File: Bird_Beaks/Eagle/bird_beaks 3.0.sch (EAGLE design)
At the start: 29 parts, among them U1 ADAFRUIT_ITSYBITSY_5V, X1 PHOENIX_508_3PIN, X10 PHOENIX_508_3PIN, X11 PHOENIX_508_4PIN, X2 PHOENIX_508_3PIN, X3 PHOENIX_508_3PIN, X4 PHOENIX_508_2PIN, X5 PHOENIX_508_4PIN, X6 PHOENIX_508_4PIN, X7 PHOENIX_508_3PIN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

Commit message: Revision for output
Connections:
- removed net HUMMINGIRD_OUTPUT: U1.SDA
- net HUMMINGBIRD_OUTPUT: now also U1.SDA
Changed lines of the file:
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@@
 <class number="0" name="Low Power" width="0.1524" drill="0.254">
 </class>
-<class number="1" name="High Power" width="0.762" drill="0.4826">
+<class number="1" name="High Power" width="1.27" drill="0.4826">
 </class>
 </classes>
@@
 </segment>
 </net>
-<net name="HUMMINGIRD_OUTPUT" class="0">
-<segment>
-<pinref part="U1" gate="G$1" pin="SDA"/>
-<wire x1="114.3" y1="134.62" x2="116.84" y2="134.62" width="0.1524" layer="91"/>
-<label x="116.84" y="134.62" size="1.778" layer="95"/>
-</segment>
-</net>
 <net name="TREECREEPER_OUTPUT" class="0">
 <segment>
@@
 </segment>
 </net>
-<net name="HUMMINGBIRD_OUTPUT" class="0">
-<segment>
-<pinref part="X9" gate="-2" pin="1"/>
-<wire x1="292.1" y1="205.74" x2="292.1" y2="195.58" width="0.1524" layer="91"/>
-<label x="289.56" y="198.12" size="1.778" layer="95" rot="R270"/>
-</segment>
-</net>
 <net name="12V" class="1">
 <segment>
@@
 </segment>
 </net>
+<net name="HUMMINGBIRD_OUTPUT" class="0">
+<segment>
+<pinref part="U1" gate="G$1" pin="SDA"/>
+<wire x1="114.3" y1="134.62" x2="116.84" y2="134.62" width="0.1524" layer="91"/>
+<label x="116.84" y="134.62" size="1.778" layer="95"/>
+</segment>
+<segment>
+<pinref part="X9" gate="-2" pin="1"/>
+<wire x1="292.1" y1="205.74" x2="292.1" y2="195.58" width="0.1524" layer="91"/>
+<label x="292.1" y="175.26" size="1.778" layer="95" rot="R90"/>
+</segment>
+</net>

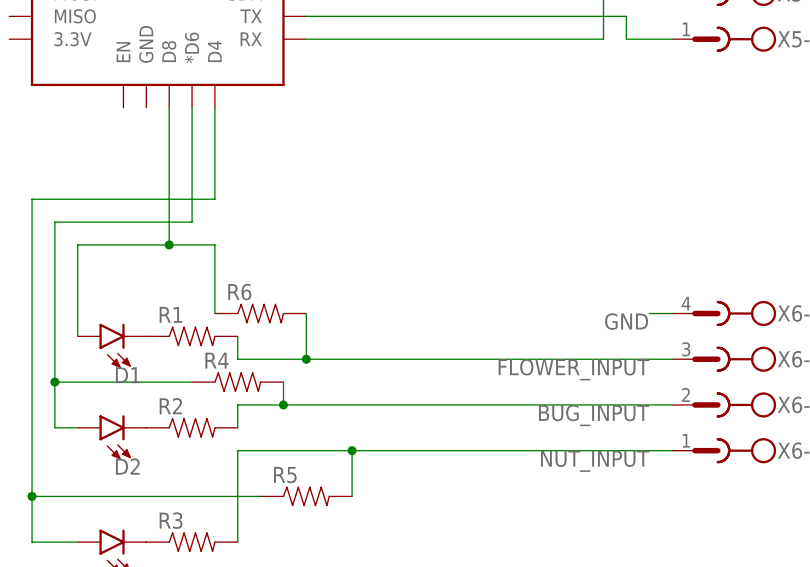
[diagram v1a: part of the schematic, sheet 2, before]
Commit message: completed the attractor sequence
fully flushed out the attractor sequence so that it will pulse on and off
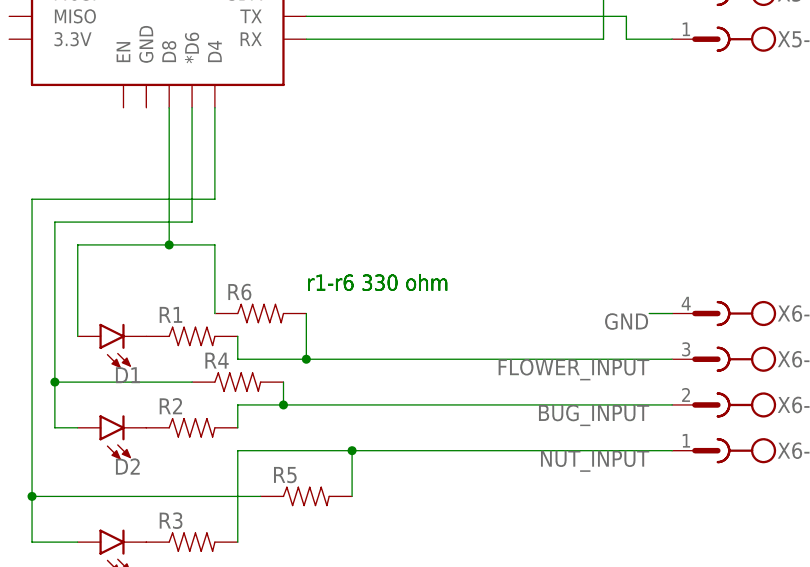
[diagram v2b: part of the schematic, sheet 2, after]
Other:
- note added: "r1-r6 330 ohm"
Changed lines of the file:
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@@
 <text x="223.52" y="228.6" size="1.778" layer="97">Bug Lighting</text>
 <text x="274.32" y="226.06" size="1.778" layer="97">Flower Lighting</text>
+<text x="114.3" y="101.6" size="1.778" layer="91">r1-r6 330 ohm</text>
+<text x="114.3" y="101.6" size="1.778" layer="91">r1-r6 330 ohm</text>
 </plain>
 <instances>
